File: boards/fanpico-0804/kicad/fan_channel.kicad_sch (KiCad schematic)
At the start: 16 parts, among them Q4 2N7002K

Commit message: PCB version 1.2
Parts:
- added TP9: TestPoint, TestPoint:TestPoint_Pad_D1.5mm, symbol Connector:TestPoint
- renumbered C18 to C15, C19 to C16, C20 to C17, D19 to D15, D20 to D16, D21 to D17, D22 to D18, JP5 to JP4, Q4 to Q3, R29 to R22, R30 to R23, R31 to R24, R32 to R25, R33 to R26, R34 to R27, R35 to R28
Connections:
- net PWR_IN: now also TP9.1
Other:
- title: FanPico-0804 -> FanPico-0804 v1.2
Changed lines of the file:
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@@
   (paper "A4")
   (title_block
-    (title "FanPico-0804")
-    (date "2022-02-26")
+    (title "FanPico-0804 v1.2")
+    (date "2022-03-11")
     (company "Timo Kokkonen <tjko@iki.fi>")
-    (comment 3 "Fanpico firmware reference/prototype PCB.")
+    (comment 3 "Fanpico firmware reference PCB.")
   )
   (junction (at 107.95 132.08) (diameter 0) (color 0 0 0 0)
@@
   (junction (at 115.57 43.18) (diameter 0) (color 0 0 0 0)
   )
+  (junction (at 88.9 132.08) (diameter 0) (color 0 0 0 0)
+  )
   (junction (at 190.5 71.12) (diameter 0) (color 0 0 0 0)
   )
@@
     (stroke (width 0) (type default) (color 0 0 0 0))
   )
-  (wire (pts (xy 68.58 132.08) (xy 107.95 132.08))
+  (wire (pts (xy 68.58 132.08) (xy 88.9 132.08))
     (stroke (width 0) (type default) (color 0 0 0 0))
   )
@@
     (stroke (width 0) (type default) (color 0 0 0 0))
   )
+  (wire (pts (xy 88.9 132.08) (xy 107.95 132.08))
+    (stroke (width 0) (type default) (color 0 0 0 0))
+  )
   (wire (pts (xy 115.57 43.18) (xy 115.57 46.99))
     (stroke (width 0) (type default) (color 0 0 0 0))
@@
   )
   (wire (pts (xy 190.5 71.12) (xy 190.5 76.2))
+    (stroke (width 0) (type default) (color 0 0 0 0))
+  )
+  (wire (pts (xy 88.9 128.27) (xy 88.9 132.08))
     (stroke (width 0) (type default) (color 0 0 0 0))
   )
@@
   (symbol (lib_id "Device:R") (at 105.41 34.29 180)
     (in_bom yes) (on_board yes) (fields_autoplaced)
-    (property "Reference" "R30" (id 0) (at 107.95 33.0199 0)
+    (property "Reference" "R23" (id 0) (at 107.95 33.0199 0)
       (effects (font (size 1.27 1.27)) (justify right))
     )
@@
   (symbol (lib_id "power:GND") (at 215.9 135.89 0)
     (in_bom yes) (on_board yes) (fields_autoplaced)
-    (property "Reference" "#PWR065" (id 0) (at 215.9 142.24 0)
+    (property "Reference" "#PWR057" (id 0) (at 215.9 142.24 0)
       (effects (font (size 1.27 1.27)) hide)
     )
@@
   (symbol (lib_id "Device:R") (at 190.5 125.73 0)
     (in_bom yes) (on_board yes) (fields_autoplaced)
-    (property "Reference" "R33" (id 0) (at 193.04 124.4599 0)
+    (property "Reference" "R26" (id 0) (at 193.04 124.4599 0)
       (effects (font (size 1.27 1.27)) (justify left))
     )
@@
   (symbol (lib_id "Device:D") (at 212.09 71.12 180)
     (in_bom yes) (on_board yes) (fields_autoplaced)
-    (property "Reference" "D21" (id 0) (at 212.09 64.77 0))
+    (property "Reference" "D17" (id 0) (at 212.09 64.77 0))
     (property "Value" "BAT54C" (id 1) (at 212.09 67.31 0))
     (property "Footprint" "Diode_SMD:D_SOT-23_ANK" (id 2) (at 212.09 71.12 0)
@@
   (symbol (lib_id "Device:R") (at 93.98 43.18 270)
     (in_bom yes) (on_board yes) (fields_autoplaced)
-    (property "Reference" "R29" (id 0) (at 93.98 36.83 90))
+    (property "Reference" "R22" (id 0) (at 93.98 36.83 90))
     (property "Value" "1k" (id 1) (at 93.98 39.37 90))
     (property "Footprint" "Resistor_SMD:R_0603_1608Metric_Pad0.98x0.95mm_HandSolder" (id 2) (at 93.98 41.402 90)
@@
   (symbol (lib_id "power:GND") (at 190.5 87.63 0)
     (in_bom yes) (on_board yes) (fields_autoplaced)
-    (property "Reference" "#PWR062" (id 0) (at 190.5 93.98 0)
+    (property "Reference" "#PWR054" (id 0) (at 190.5 93.98 0)
       (effects (font (size 1.27 1.27)) hide)
     )
@@
   (symbol (lib_id "Device:C") (at 115.57 50.8 0)
     (in_bom yes) (on_board yes) (fields_autoplaced)
-    (property "Reference" "C18" (id 0) (at 119.38 49.5299 0)
+    (property "Reference" "C15" (id 0) (at 119.38 49.5299 0)
       (effects (font (size 1.27 1.27)) (justify left))
     )
@@
   (symbol (lib_id "Transistor_FET:2N7002K") (at 104.14 88.9 0)
     (in_bom yes) (on_board yes) (fields_autoplaced)
-    (property "Reference" "Q4" (id 0) (at 110.49 87.6299 0)
+    (property "Reference" "Q3" (id 0) (at 110.49 87.6299 0)
       (effects (font (size 1.27 1.27)) (justify left))
     )
@@
   (symbol (lib_id "power:+3.3V") (at 115.57 26.67 270)
     (in_bom yes) (on_board yes) (fields_autoplaced)
-    (property "Reference" "#PWR060" (id 0) (at 111.76 26.67 0)
+    (property "Reference" "#PWR052" (id 0) (at 111.76 26.67 0)
       (effects (font (size 1.27 1.27)) hide)
     )
@@
   (symbol (lib_id "Device:C") (at 190.5 80.01 0)
     (in_bom yes) (on_board yes) (fields_autoplaced)
-    (property "Reference" "C19" (id 0) (at 194.31 78.7399 0)
+    (property "Reference" "C16" (id 0) (at 194.31 78.7399 0)
       (effects (font (size 1.27 1.27)) (justify left))
     )
@@
   (symbol (lib_id "power:GND") (at 115.57 55.88 0)
     (in_bom yes) (on_board yes) (fields_autoplaced)
-    (property "Reference" "#PWR061" (id 0) (at 115.57 62.23 0)
+    (property "Reference" "#PWR053" (id 0) (at 115.57 62.23 0)
       (effects (font (size 1.27 1.27)) hide)
     )
@@
   (symbol (lib_id "power:+3.3V") (at 194.31 57.15 90)
     (in_bom yes) (on_board yes) (fields_autoplaced)
-    (property "Reference" "#PWR064" (id 0) (at 198.12 57.15 0)
+    (property "Reference" "#PWR056" (id 0) (at 198.12 57.15 0)
       (effects (font (size 1.27 1.27)) hide)
     )
@@
   (symbol (lib_id "power:GND") (at 190.5 144.78 0)
     (in_bom yes) (on_board yes) (fields_autoplaced)
-    (property "Reference" "#PWR063" (id 0) (at 190.5 151.13 0)
+    (property "Reference" "#PWR055" (id 0) (at 190.5 151.13 0)
       (effects (font (size 1.27 1.27)) hide)
     )
@@
   (symbol (lib_id "Device:R") (at 116.84 80.01 90)
     (in_bom yes) (on_board yes)
-    (property "Reference" "R32" (id 0) (at 116.84 82.55 90))
+    (property "Reference" "R25" (id 0) (at 116.84 82.55 90))
     (property "Value" "1k" (id 1) (at 116.84 85.09 90))
     (property "Footprint" "Resistor_SMD:R_0603_1608Metric_Pad0.98x0.95mm_HandSolder" (id 2) (at 116.84 81.788 90)
@@
   (symbol (lib_id "Device:LED") (at 190.5 135.89 90)
     (in_bom yes) (on_board yes)
-    (property "Reference" "D20" (id 0) (at 185.42 135.89 90)
+    (property "Reference" "D16" (id 0) (at 185.42 135.89 90)
       (effects (font (size 1.27 1.27)) (justify right))
     )
@@
   (symbol (lib_id "power:GND") (at 106.68 97.79 0)
     (in_bom yes) (on_board yes) (fields_autoplaced)
-    (property "Reference" "#PWR058" (id 0) (at 106.68 104.14 0)
+    (property "Reference" "#PWR050" (id 0) (at 106.68 104.14 0)
       (effects (font (size 1.27 1.27)) hide)
     )
@@
   (symbol (lib_id "Device:R") (at 200.66 63.5 180)
     (in_bom yes) (on_board yes) (fields_autoplaced)
-    (property "Reference" "R34" (id 0) (at 203.2 62.2299 0)
+    (property "Reference" "R27" (id 0) (at 203.2 62.2299 0)
       (effects (font (size 1.27 1.27)) (justify right))
     )
@@
   (symbol (lib_id "power:GND") (at 107.95 158.75 0)
     (in_bom yes) (on_board yes) (fields_autoplaced)
-    (property "Reference" "#PWR059" (id 0) (at 107.95 165.1 0)
+    (property "Reference" "#PWR051" (id 0) (at 107.95 165.1 0)
       (effects (font (size 1.27 1.27)) hide)
     )
@@
   (symbol (lib_id "Device:D") (at 215.9 125.73 270)
     (in_bom yes) (on_board yes) (fields_autoplaced)
-    (property "Reference" "D22" (id 0) (at 218.44 124.4599 90)
+    (property "Reference" "D18" (id 0) (at 218.44 124.4599 90)
       (effects (font (size 1.27 1.27)) (justify left))
     )
@@
   (symbol (lib_id "Jumper:Jumper_3_Bridged12") (at 175.26 118.11 90)
     (in_bom yes) (on_board yes) (fields_autoplaced)
-    (property "Reference" "JP5" (id 0) (at 172.72 116.8399 90)
+    (property "Reference" "JP4" (id 0) (at 172.72 116.8399 90)
       (effects (font (size 1.27 1.27)) (justify left))
     )
@@
   (symbol (lib_id "Device:C") (at 204.47 125.73 0)
     (in_bom yes) (on_board yes) (fields_autoplaced)
-    (property "Reference" "C20" (id 0) (at 208.28 124.4599 0)
+    (property "Reference" "C17" (id 0) (at 208.28 124.4599 0)
       (effects (font (size 1.27 1.27)) (justify left))
     )
@@
   (symbol (lib_id "Device:R") (at 107.95 139.7 0)
     (in_bom yes) (on_board yes) (fields_autoplaced)
-    (property "Reference" "R31" (id 0) (at 110.49 138.4299 0)
+    (property "Reference" "R24" (id 0) (at 110.49 138.4299 0)
       (effects (font (size 1.27 1.27)) (justify left))
     )
@@
     (pin "2")
   )
+  (symbol (lib_id "Connector:TestPoint") (at 88.9 128.27 0)
+    (in_bom yes) (on_board yes) (fields_autoplaced)
+    (property "Reference" "TP9" (id 0) (at 91.44 123.6979 0)
+      (effects (font (size 1.27 1.27)) (justify left))
+    )
+    (property "Value" "TestPoint" (id 1) (at 91.44 126.2379 0)
+      (effects (font (size 1.27 1.27)) (justify left))
+    )
+    (property "Footprint" "TestPoint:TestPoint_Pad_D1.5mm" (id 2) (at 93.98 128.27 0)
+      (effects (font (size 1.27 1.27)) hide)
+    )
+    (property "Datasheet" "~" (id 3) (at 93.98 128.27 0)
+      (effects (font (size 1.27 1.27)) hide)
+    )
+    (pin "1")
+  )
   (symbol (lib_id "Device:LED") (at 107.95 149.86 90)
     (in_bom yes) (on_board yes) (fields_autoplaced)
-    (property "Reference" "D19" (id 0) (at 111.76 150.1774 90)
+    (property "Reference" "D15" (id 0) (at 111.76 150.1774 90)
       (effects (font (size 1.27 1.27)) (justify right))
     )
@@
   (symbol (lib_id "Device:R") (at 201.93 43.18 90)
     (in_bom yes) (on_board yes) (fields_autoplaced)
-    (property "Reference" "R35" (id 0) (at 201.93 36.83 90))
+    (property "Reference" "R28" (id 0) (at 201.93 36.83 90))
     (property "Value" "680" (id 1) (at 201.93 39.37 90))
     (property "Footprint" "Resistor_SMD:R_0603_1608Metric_Pad0.98x0.95mm_HandSolder" (id 2) (at 201.93 44.958 90)

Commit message: New PCB revision v1.3
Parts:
- renumbered C16 to C10, C17 to C11, C15 to C9, D18 to D10, D15 to D7, D16 to D8, D17 to D9, JP4 to JP2, Q3 to Q1, R24 to R10, R25 to R11, R26 to R12, R27 to R13, R28 to R14, R22 to R8, R23 to R9, TP9 to TP6
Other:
- title: FanPico-0804 v1.2 -> FanPico-0804 v1.3

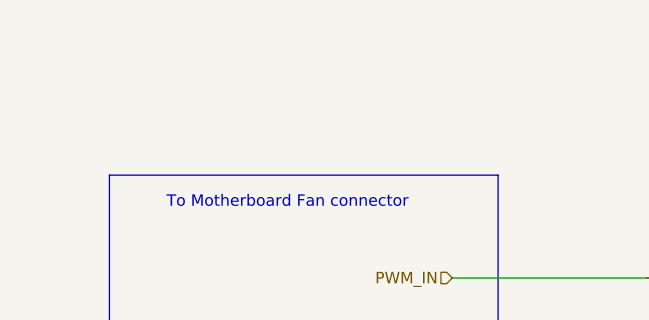
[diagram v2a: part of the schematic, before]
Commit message: Cleanup schematic (no actual changes that affect PCB).
- Add labels to sub-pages so printed schematic is more readable.
- Rename FANx_PWM_READ to MBFANx_PWM_READ
- Rename FANx_TACHO_GEN to MBFANx_TACHO_GEN
- Use standard (KiCAD) footprints for the ICs (U1-U3)
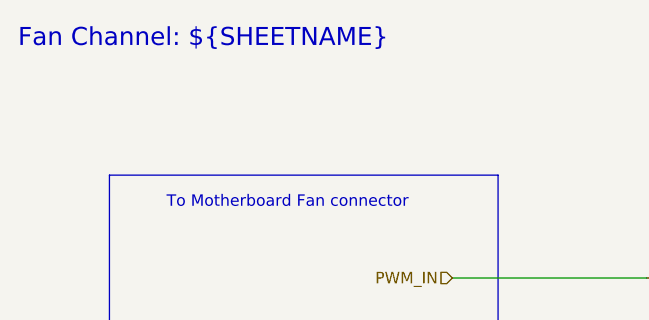
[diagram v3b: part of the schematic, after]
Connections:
- net +3V3 renamed +3.3V
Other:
- note added: "Fan Channel: ${SHEETNAME}"
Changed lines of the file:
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@@
   (title_block
     (title "FanPico-0804 v1.3")
-    (date "2022-04-10")
+    (date "2022-08-18")
     (company "Timo Kokkonen <tjko@iki.fi>")
     (comment 3 "Fanpico firmware reference PCB.")
@@
     (effects (font (size 1.27 1.27)) (justify left bottom))
   )
+  (text "Fan Channel: ${SHEETNAME}" (at 20.32 17.78 0)
+    (effects (font (size 2 2)) (justify left bottom))
+  )
   (text "To Fan" (at 243.84 35.56 0)
